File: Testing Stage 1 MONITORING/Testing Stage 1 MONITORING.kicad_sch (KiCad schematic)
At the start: 78 parts, among them J1 Conn_01x06_Socket, J2 Conn_01x03_Pin, Q1 PMOS, Q2 NMOS, Q3 AO3401A, Q4 BUK7M67-60EX, Q5 BUK7M67-60EX, SW1 SW_Push, U1 BQ76920PW, U2 BQ78350DBT, U3 BQ76200PW

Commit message: need to fix high side control IC - no need for precharge system
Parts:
- added J3: Conn_01x02, TerminalBlock_CUI:TerminalBlock_CUI_TB007-508-02_1x02_P5.08mm_Horizontal, symbol Connector_Generic:Conn_01x02
- renumbered Cfilter_HS_SW_BAT1 to C14, C14 to C15, CVDDCP_HS_SW1 to C16, Cfilter1 to C17, Rd_AFE_REGSRC1 to R15, R15 to R16, R16 to R17, R17 to R18, R18 to R19, R19 to R20, R20 to R21, R21 to R22, R22 to R23, R23 to R24, R24 to R25, Rpchg_HS_SW1 to R26, R25 to R27, Rfilter_HS_SW_BAT1 to R28, R26 to R29, RGS_HS_SW_PCHG1 to R30, R27 to R31, R28 to R32, R29 to R33, R30 to R34, R_filter1 to R35
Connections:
- net GND: now also J3.2 (Pin_2)
- net PACK+: now also J3.1 (Pin_1)

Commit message: fixed schematic, changed high side FETs, rough layout, still need to change footprints to 0805 so can be manufactured cheap at uni
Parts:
- removed Q3: AO3401A, Package_TO_SOT_SMD:SOT-23, symbol Transistor_FET:AO3401A
- removed Q4, Q5: BUK7M67-60EX, Package_TO_SOT_SMD:LFPAK33, symbol Transistor_FET:BUK7M67-60EX
- removed R30: 10M, Resistor_SMD:R_1210_3225Metric_Pad1.30x2.65mm_HandSolder, symbol Device:R
- removed R34: 16k, Resistor_SMD:R_1210_3225Metric_Pad1.30x2.65mm_HandSolder, symbol Device:R
- removed R35: 100, Resistor_SMD:R_1210_3225Metric_Pad1.30x2.65mm_HandSolder, symbol Device:R
- added Q5, Q6: NMOS, Package_TO_SOT_THT:TO-220-3_Vertical, symbol Simulation_SPICE:NMOS
- added R31: 300k, Resistor_SMD:R_1210_3225Metric_Pad1.30x2.65mm_HandSolder, symbol Device:R
- C17: value 0.01u -> 10n
- R26: value 10M -> 100
- R28: value 100 -> 10M
- R32: value 10M -> 16k
- R33: value 300k -> 100
- renumbered R31 to R30
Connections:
- net BATT+: now also Q5.3 (S)
- net CHG_GATE: now also R28.2, Q5.2 (G); no longer R29.2
- net DSG_GATE: now also R29.2, Q6.2 (G); no longer R32.2
- net GND: now also R32.2
- net HS_SW_PACKDIV: now also R32.1, R31.2; no longer R33.2
- net PACK+: now also R29.1, R33.2, Q6.3 (S); no longer R32.1
- net at C17.2, U3.11 (PACK): now also R33.1
- net at U3.10 (PACKDIV): now also R31.1; no longer R33.1
- net at C14.2, C16.2, U3.2 (BAT): now also R26.2; no longer R28.2
- net PCHG_GATE: no longer names the net of U3.14 (PCHG)
- new net: Q5.1 (D), Q6.1 (D)
- no-connect marks 3 -> 4
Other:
- note added: "STP36NF06L"
- note added: "not using precharge function"
- moved on the sheet: J3

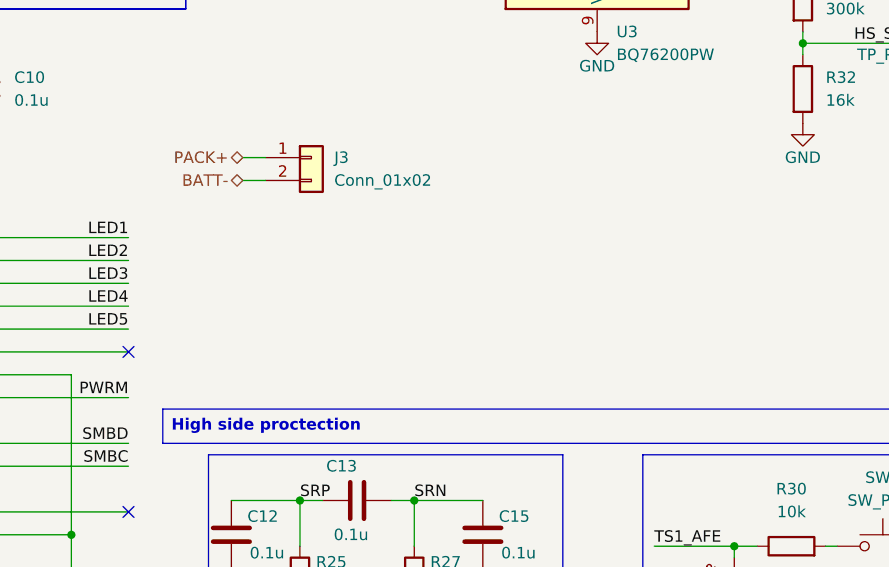
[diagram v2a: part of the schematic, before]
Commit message: routing and layout updates
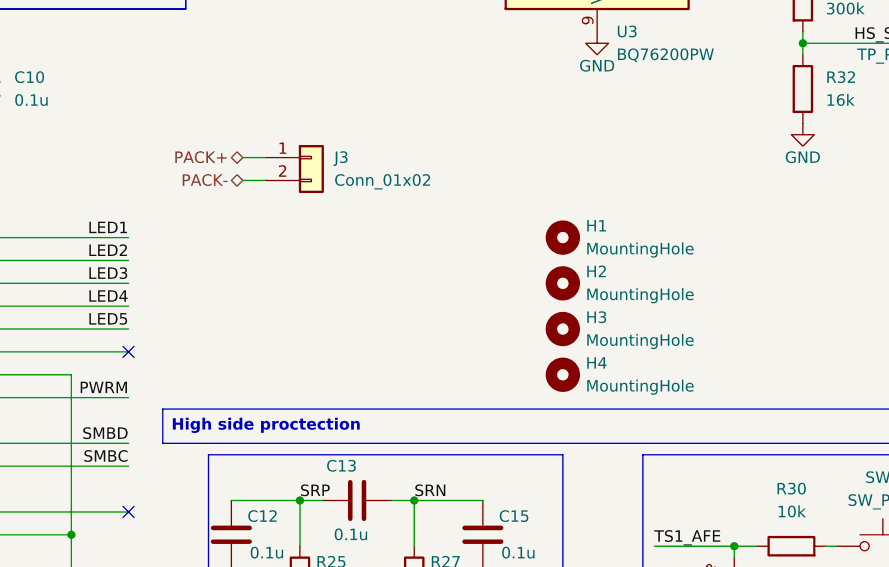
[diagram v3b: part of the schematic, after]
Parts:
- added H1, H2, H3, H4: MountingHole, MountingHole:MountingHole_3.2mm_M3, symbol Mechanical:MountingHole
- C1, C10, C11, C12, C13, C14, C15, C16, C17, C2, C3, C4, C5, C6, C7, C8, C9, Cf1: footprint Capacitor_SMD:C_1210_3225Metric_Pad1.33x2.70mm_HandSolder -> Capacitor_SMD:C_0805_2012Metric_Pad1.18x1.45mm_HandSolder
- R1, R10, R11, R12, R13, R14, R15, R16, R17, R18, R19, R2, R20, R21, R22, R23, R24, R25, R26, R27, R28, R29, R3, R30, R31, R32, R33, R4, R5, R6, R7, R8, R9, Rf_AFE_BATT1, TH1: footprint Resistor_SMD:R_1210_3225Metric_Pad1.30x2.65mm_HandSolder -> Resistor_SMD:R_0805_2012Metric_Pad1.20x1.40mm_HandSolder
- Rsense1: footprint Resistor_SMD:R_1206_3216Metric_Pad1.30x1.75mm_HandSolder -> Resistor_SMD:R_0805_2012Metric_Pad1.20x1.40mm_HandSolder
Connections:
- net GND: no longer J3.2 (Pin_2)
- net PACK-: now also J3.2 (Pin_2)

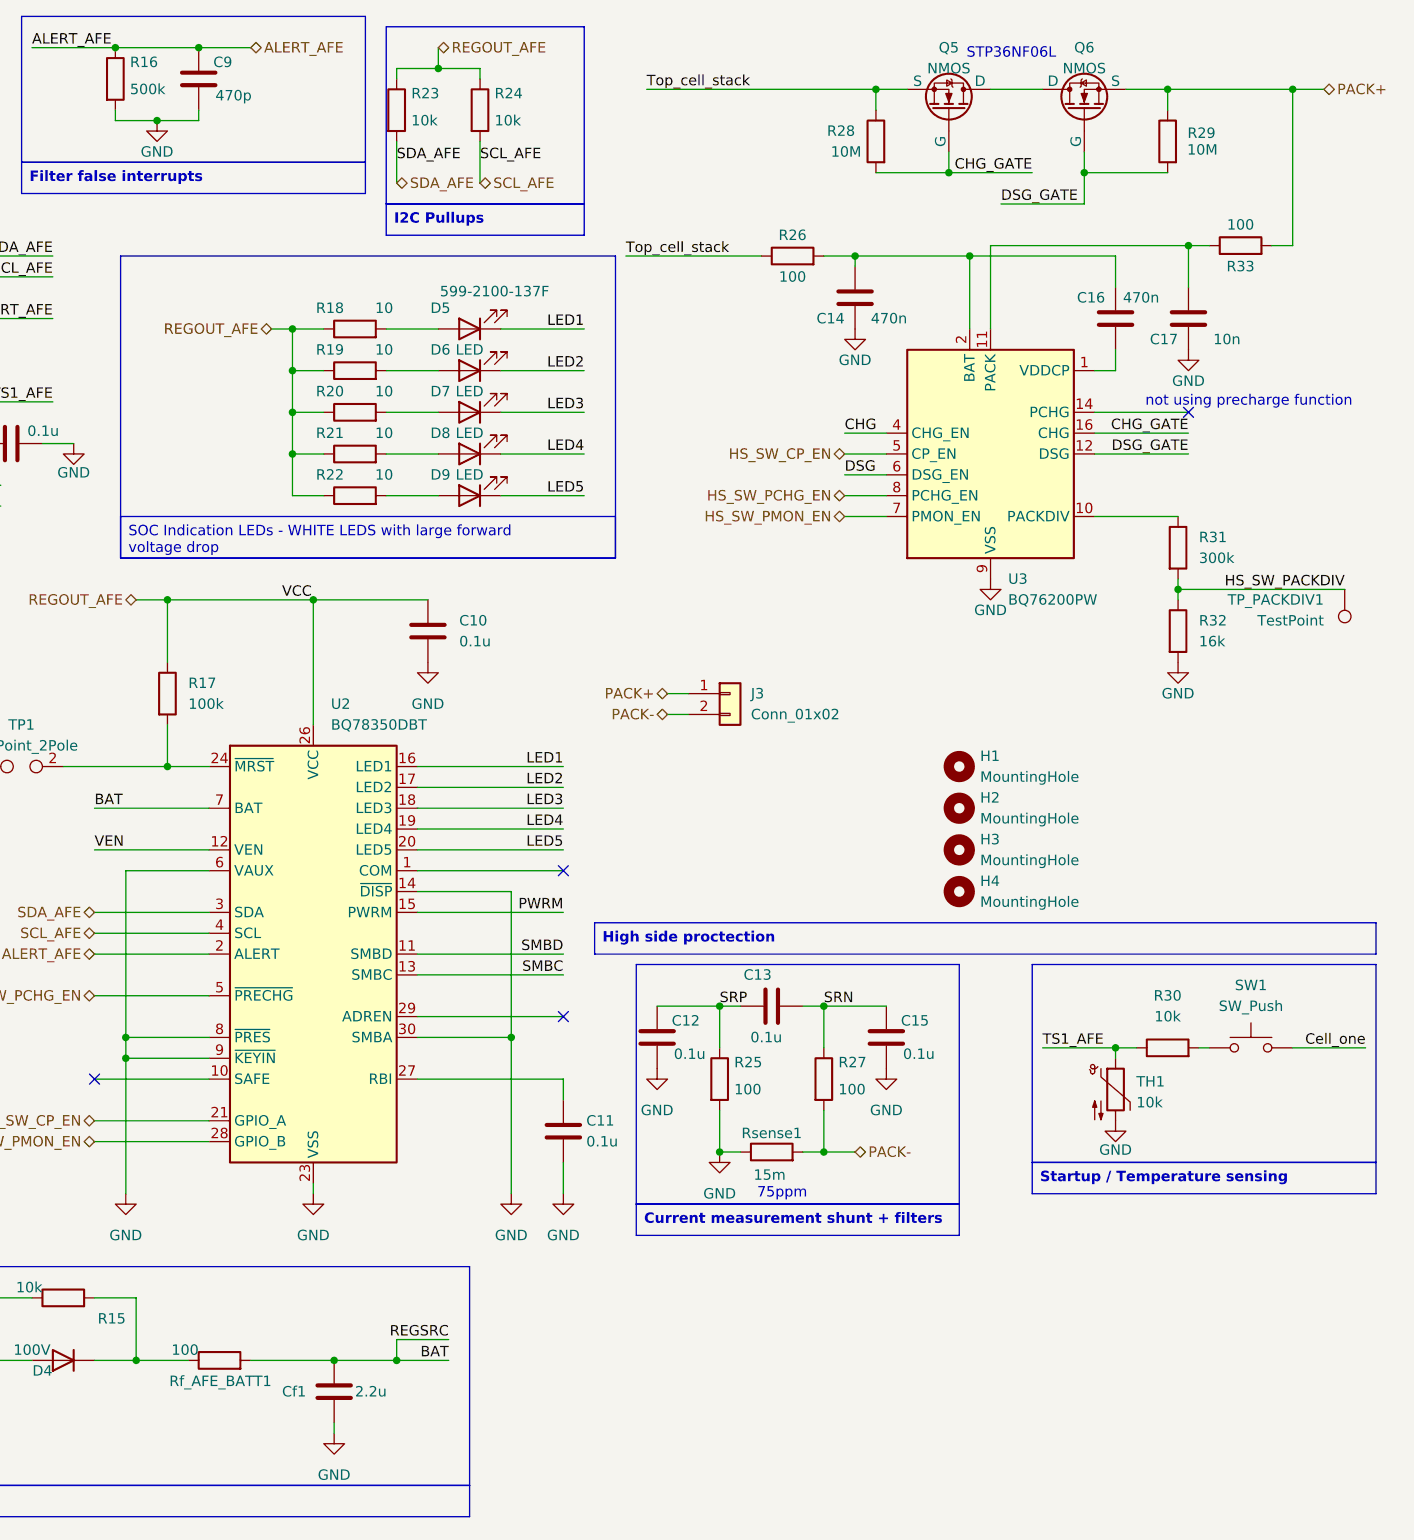
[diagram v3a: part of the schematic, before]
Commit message: updated layout and almost complete routing - need to address DRC
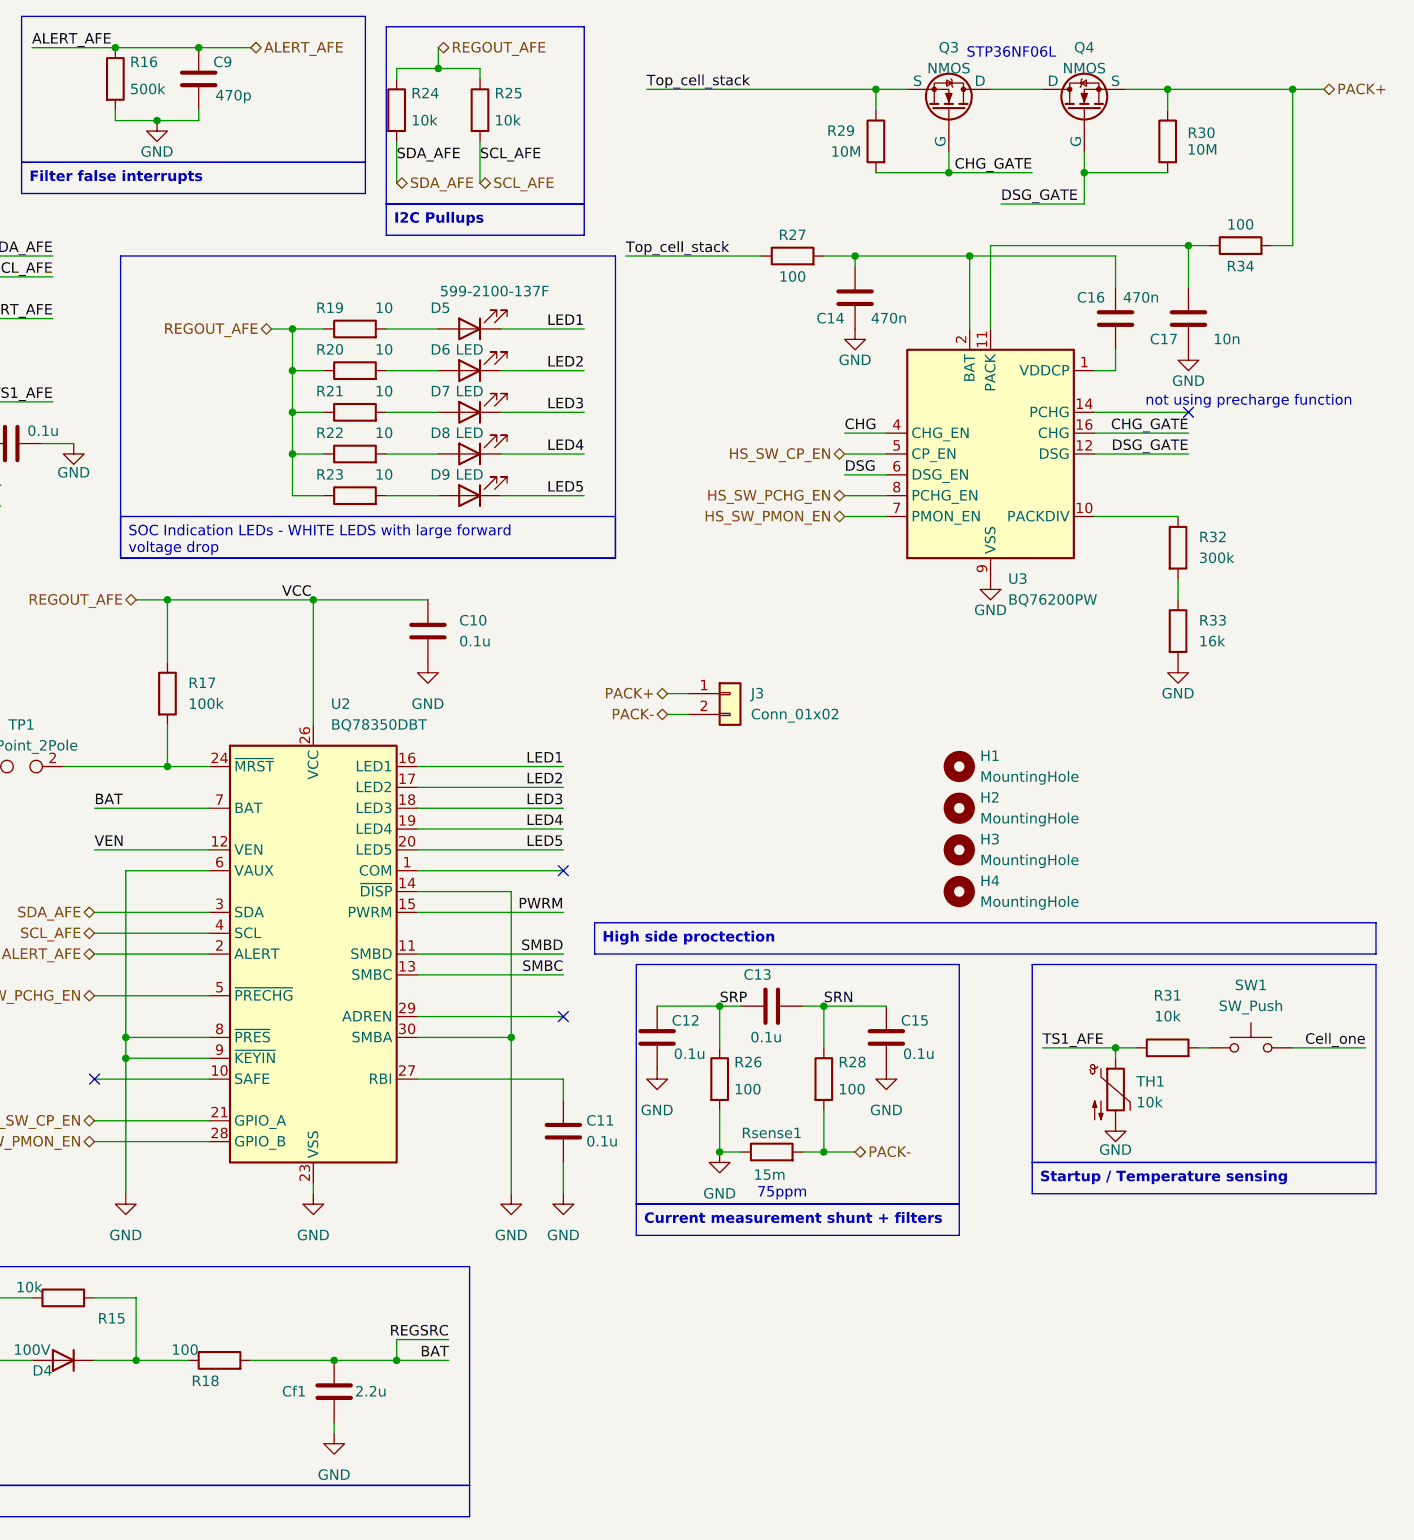
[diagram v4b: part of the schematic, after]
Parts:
- removed TP_PACKDIV1: TestPoint, TestPoint:TestPoint_Pad_2.0x2.0mm, symbol Connector:TestPoint
- renumbered Q5 to Q3, Q6 to Q4, Rf_AFE_BATT1 to R18, R18 to R19, R19 to R20, R20 to R21, R21 to R22, R22 to R23, R23 to R24, R24 to R25, R25 to R26, R26 to R27, R27 to R28, R28 to R29, R29 to R30, R30 to R31, R31 to R32, R32 to R33, R33 to R34
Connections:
- net HS_SW_PACKDIV: no longer names the net of R32.2, R33.1
